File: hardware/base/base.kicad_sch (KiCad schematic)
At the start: 70 parts, among them J1 SWD, J2 USB_B_Mini, J4 Serial Interface, J5 Debug, J5 OLED Display, J6 Conn_01x02_Pin, M1 Fan_ALT, Q1 Q_NMOS_GSD, Q2 Q_NMOS_GSD, Q3 Q_NMOS_GSD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

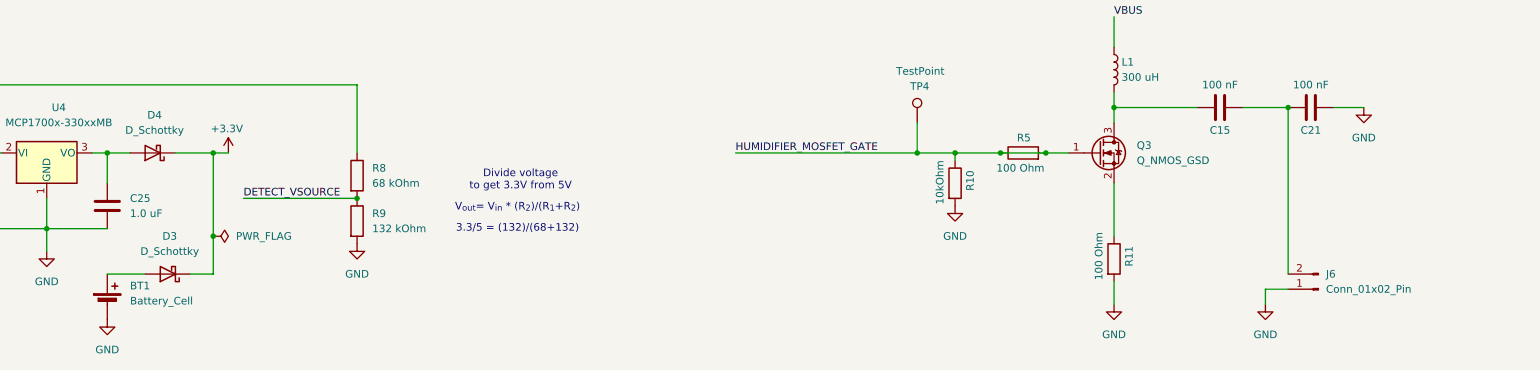
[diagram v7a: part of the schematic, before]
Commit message: Change transducer symbol
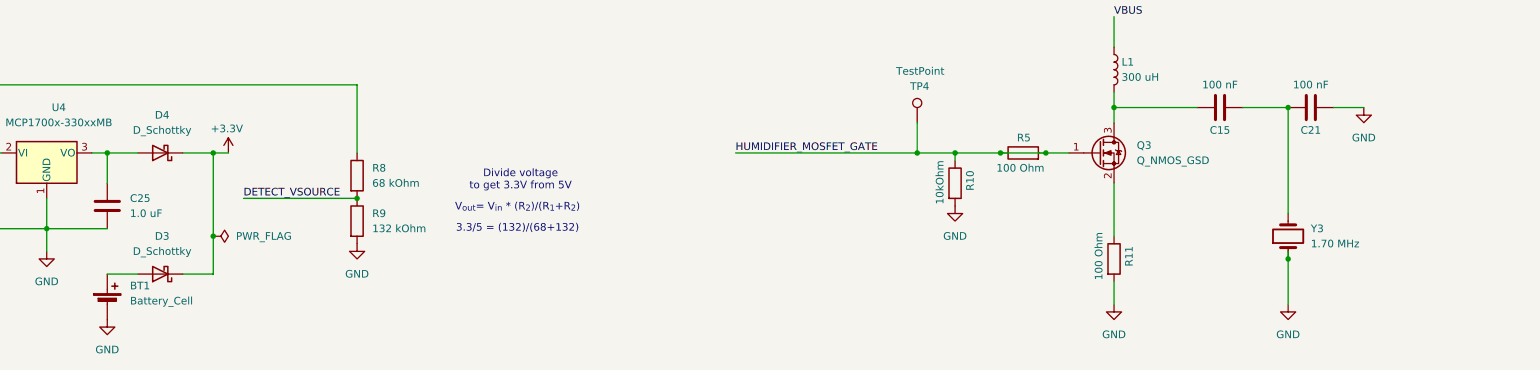
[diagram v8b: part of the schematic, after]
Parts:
- removed J6: Conn_01x02_Pin, Connector_PinHeader_2.54mm:PinHeader_1x02_P2.54mm_Vertical, symbol Connector:Conn_01x02_Pin
- added Y3: 1.70 MHz, Connector_PinHeader_2.54mm:PinHeader_1x02_P2.54mm_Vertical, symbol Device:Crystal
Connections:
- net GND: now also Y3.1
- net at C15.2, C21.1: now also Y3.2
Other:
- moved on the sheet: D3, D4
